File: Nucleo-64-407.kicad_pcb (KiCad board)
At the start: 2 copper layers, 70 x 81 mm, 70 parts, among them J1 SWD, J2 Micro_SD_Card_Det, J3 USB_B_Micro, J4 Serial 0, J5 EXP1, J6 EXP2, J7 EXP3, J8 EXP4, SW1 RESET, SW2 BOOT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

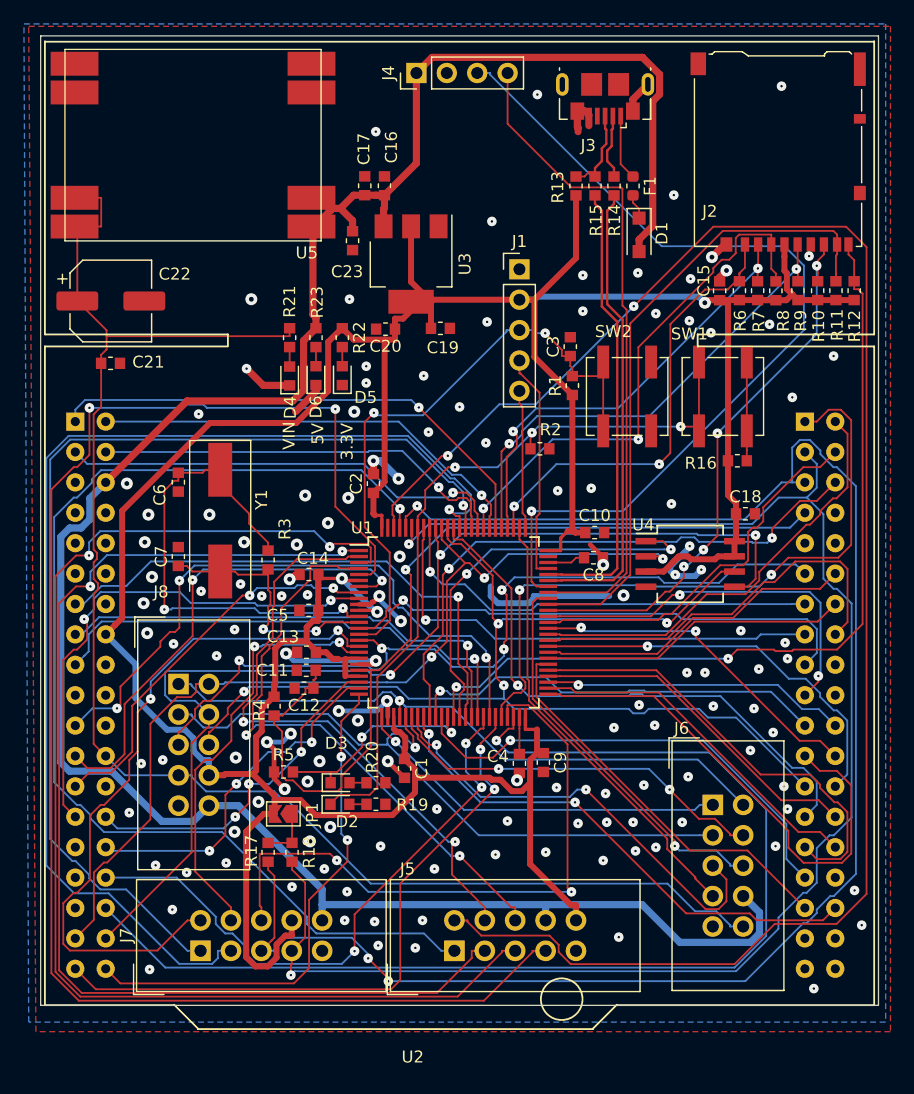
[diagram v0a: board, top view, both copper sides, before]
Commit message: Ordered rev1 of the Nucleo-64 board.
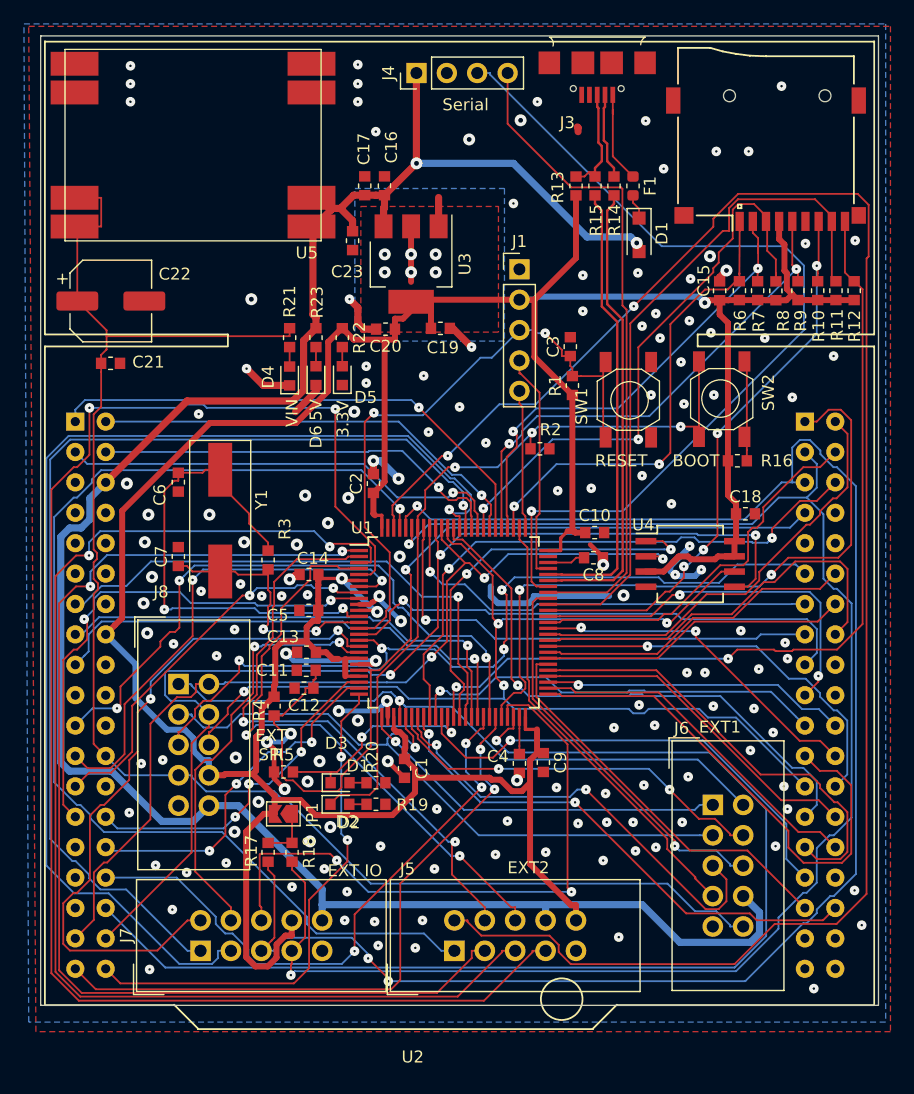
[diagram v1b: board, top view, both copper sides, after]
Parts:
- removed J2: Micro_SD_Card_Det, Connector_Card:microSD_HC_Hirose_DM3AT-SF-PEJM5
- added XS1: MicroSD, PrntrBoardV1:Conn_uSDcard, F.Cu at (113.6, 40.0)
- J3: footprint Connector_USB:USB_Micro-B_GCT_USB3076-30-A -> PrntrBoardV1:MC-101C
- SW1, SW2: footprint Button_Switch_SMD:SW_SPST_B3SL-1002P -> PrntrBoardV1:Button 4x4
- moved SW2 3.92 mm to (108.0, 68.5)
- moved SW1 3.50 mm to (104.0, 62.2)
- moved J3 1.20 mm to (99.5, 39.2)
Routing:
- net /5V: track 195.0 -> 180.0 mm, vias 0 -> 2
- net /IOE_1: track 144.7 -> 149.7 mm
- net /SDIO_CMD: track 44.7 -> 49.3 mm
- net /SDIO_D1: track 53.4 -> 57.3 mm
- net /SDIO_D3: track 37.7 -> 40.6 mm
- net Net-(F1-Pad1): track 5.47 -> 7.85 mm
- net /D+: track 7.21 -> 9.31 mm
- net /SDIO_CLK: track 40.7 -> 42.7 mm
- net /SD_DETECT: track 71.2 -> 73.1 mm
- net /SDIO_D0: track 46.6 -> 48.4 mm
- net /D-: track 5.48 -> 7.22 mm
- net /SDIO_D2: track 38.1 -> 39.9 mm
- net /3.3V: track 316.1 -> 317.8 mm, vias 3 -> 9
- net GND: track 71.2 -> 71.9 mm, vias 134 -> 153
- added copper zone on B.Cu, net /3.3V
- added copper zone on F.Cu, net /3.3V
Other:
- board text added: "BOOT"
- board text added: "D1"
- board text added: "D2"
- board text added: "EXT IO"
- board text added: "IOA 3,5,7,15"
- board text added: "IOA 4"
- board text added: "IOA 4,6,8"
- board text added: "IOA 5"
- board text added: "IOE 0,2,4,6"
- board text added: "IOE 1,3,5"
- board text added: "MISO"
- board text added: "MOSI"
- board text added: "RESET"
- board text added: "SCK"
- board text added: "SCL"
- board text added: "SDA"
- board text added: "Serial"
- board text added: "~EN_MOT"

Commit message: Make the NUCLEO-64-F407 board with rounded corners.
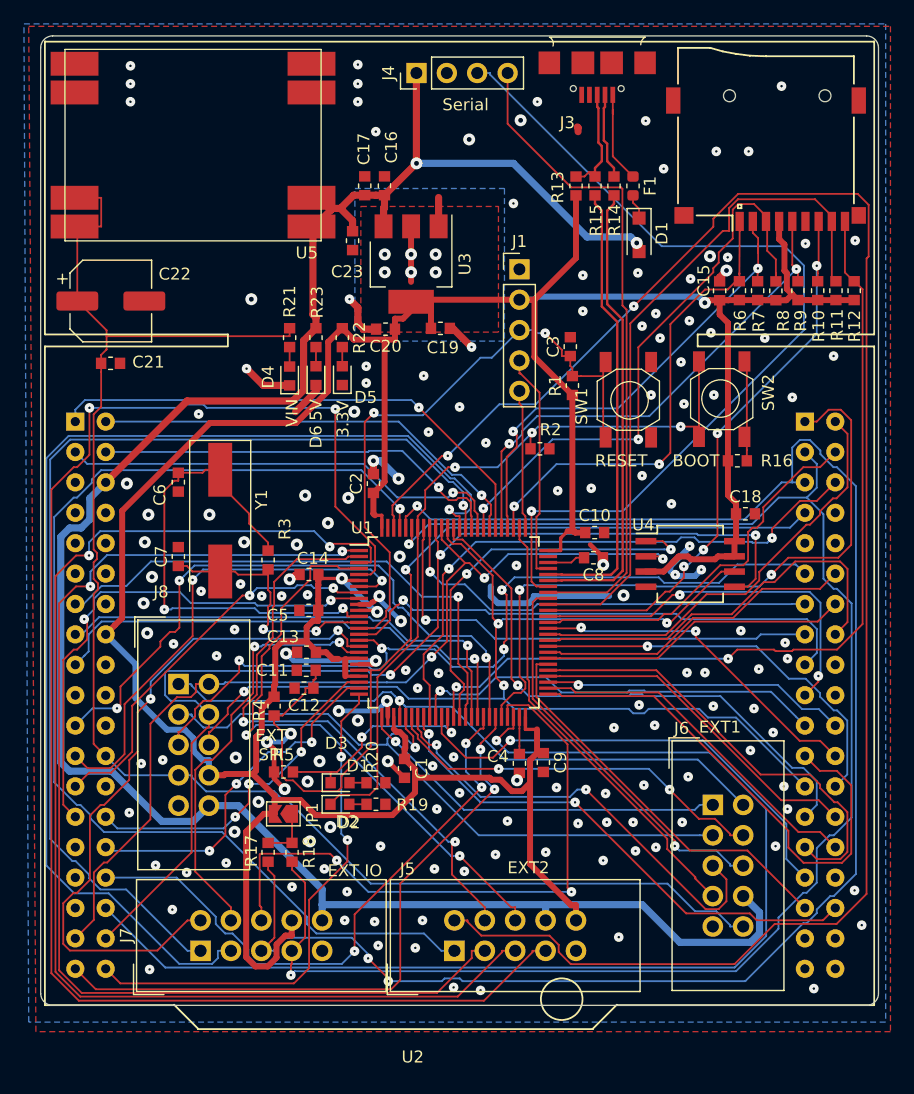
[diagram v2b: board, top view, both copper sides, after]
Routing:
- net GND: vias 153 -> 164
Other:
- outline, holes or cut-outs redrawn
- board text added: "(c) iQury.us Dec 2018"
- board text added: "Rev 2"
- board text removed: "(c) iQury.us Nov 2018"
- board text removed: "Rev1"
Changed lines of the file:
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@@
-(kicad_pcb (version 20171130) (host pcbnew 6.0.0-rc1-unknown-82f657e~66~ubuntu18.10.1)
+(kicad_pcb (version 20171130) (host pcbnew 6.0.0-rc1-unknown-0bceb69~66~ubuntu18.10.1)
   (general
     (thickness 1.6)
-    (drawings 62)
-    (tracks 1999)
+    (drawings 66)
+    (tracks 2014)
     (zones 0)
     (modules 70)
@@
     (via_min_size 0.8)
     (via_min_drill 0.2)
+    (user_via 0.8 0.2)
+    (user_via 1 0.4)
     (uvia_size 0.3)
     (uvia_drill 0.1)
@@
     )
   )
+  (gr_arc (start 54 115) (end 53 115) (angle -90) (layer Edge.Cuts) (width 0.05))
+  (gr_arc (start 122 115) (end 122 116) (angle -90) (layer Edge.Cuts) (width 0.05))
+  (gr_arc (start 122 36) (end 123 36) (angle -90) (layer Edge.Cuts) (width 0.05))
+  (gr_arc (start 54 36) (end 54 35) (angle -90) (layer Edge.Cuts) (width 0.05))
   (gr_text "EXT\nSPI" (at 72.25 94.25) (layer F.SilkS)
     (effects (font (size 1 1) (thickness 0.15)))
@@
     (effects (font (size 1 1) (thickness 0.15)) (justify mirror))
   )
-  (gr_text Rev1 (at 114.2 42) (layer B.SilkS)
+  (gr_text "Rev 2" (at 114.2 42) (layer B.SilkS)
     (effects (font (size 1.5 1.5) (thickness 0.3)) (justify mirror))
   )
-  (gr_text "(c) iQury.us\nNov 2018" (at 66.6 51.3) (layer B.SilkS)
+  (gr_text "(c) iQury.us\nDec 2018" (at 66.6 51.3) (layer B.SilkS)
     (effects (font (size 1.5 1.5) (thickness 0.3)) (justify mirror))
   )
@@
     (effects (font (size 1.5 1.5) (thickness 0.3)) (justify mirror))
   )
-  (gr_line (start 53 116) (end 53 35) (layer Edge.Cuts) (width 0.05))
-  (gr_line (start 123 116) (end 53 116) (layer Edge.Cuts) (width 0.05))
-  (gr_line (start 123 35) (end 123 116) (layer Edge.Cuts) (width 0.05))
-  (gr_line (start 53 35) (end 123 35) (layer Edge.Cuts) (width 0.05))
+  (gr_line (start 53 115) (end 53 36) (layer Edge.Cuts) (width 0.05))
+  (gr_line (start 122 116) (end 54 116) (layer Edge.Cuts) (width 0.05))
+  (gr_line (start 123 36) (end 123 115) (layer Edge.Cuts) (width 0.05))
+  (gr_line (start 54 35) (end 122 35) (layer Edge.Cuts) (width 0.05))
   (segment (start 94.2 81.8) (end 94.2 82) (width 0.5) (layer B.Cu) (net 1))
   (segment (start 94.2 82) (end 93.8 82.4) (width 0.5) (layer B.Cu) (net 1))
@@
   (via (at 104.75 60.25) (size 0.8) (drill 0.2) (layers F.Cu B.Cu) (net 1))
   (via (at 103.25 59.25) (size 0.8) (drill 0.2) (layers F.Cu B.Cu) (net 1))
+  (via (at 89.75 114.75) (size 0.8) (drill 0.2) (layers F.Cu B.Cu) (net 1))
+  (via (at 87.5 114.5) (size 0.8) (drill 0.2) (layers F.Cu B.Cu) (net 1))
+  (via (at 88 98.25) (size 0.8) (drill 0.2) (layers F.Cu B.Cu) (net 1))
+  (via (at 85.75 96) (size 0.8) (drill 0.2) (layers F.Cu B.Cu) (net 1))
+  (via (at 87.5 95.25) (size 0.8) (drill 0.2) (layers F.Cu B.Cu) (net 1))
+  (via (at 84.5 89.5) (size 0.8) (drill 0.2) (layers F.Cu B.Cu) (net 1))
+  (via (at 83.5 88) (size 0.8) (drill 0.2) (layers F.Cu B.Cu) (net 1))
+  (via (at 86.25 88.25) (size 0.8) (drill 0.2) (layers F.Cu B.Cu) (net 1))
+  (via (at 92.75 79.25) (size 0.8) (drill 0.2) (layers F.Cu B.Cu) (net 1))
+  (via (at 88.4 104.8) (size 0.8) (drill 0.2) (layers F.Cu B.Cu) (net 1))
+  (via (at 110.4 53.5) (size 0.8) (drill 0.2) (layers F.Cu B.Cu) (net 1))
   (segment (start 95.4 78) (end 96.4426 78) (width 0.2798) (layer F.Cu) (net 2))
   (segment (start 97.0174 76.3826) (end 96.4426 76.9574) (width 0.2798) (layer F.Cu) (net 2))
@@
   (via (at 97.3457 106.5181) (size 0.8) (layers F.Cu B.Cu) (net 40))
   (segment (start 115.7899 72.305) (end 116.8515 72.305) (width 0.1524) (layer B.Cu) (net 41))
-  (segment (start 82.0448 113.9811) (end 111.8717 113.9811) (width 0.1524) (layer B.Cu) (net 41))
-  (segment (start 111.8717 113.9811) (end 116.7178 109.135) (width 0.1524) (layer B.Cu) (net 41))
-  (segment (start 116.7178 109.135) (end 117.0008 109.135) (width 0.1524) (layer B.Cu) (net 41))
-  (segment (start 117.0008 109.135) (end 117.8426 108.2932) (width 0.1524) (layer B.Cu) (net 41))
-  (segment (start 117.8426 108.2932) (end 117.8426 107.9947) (width 0.1524) (layer B.Cu) (net 41))
-  (segment (start 117.8426 107.9947) (end 118.9634 106.8739) (width 0.1524) (layer B.Cu) (net 41))
-  (segment (start 118.9634 106.8739) (end 119.2567 106.8739) (width 0.1524) (layer B.Cu) (net 41))
-  (segment (start 119.2567 106.8739) (end 121.114 105.0166) (width 0.1524) (layer B.Cu) (net 41))
-  (segment (start 121.114 105.0166) (end 121.114 72.6223) (width 0.1524) (layer B.Cu) (net 41))
-  (segment (start 121.114 72.6223) (end 119.5267 71.035) (width 0.1524) (layer B.Cu) (net 41))
-  (segment (start 119.5267 71.035) (end 119.2413 71.035) (width 0.1524) (layer B.Cu) (net 41))
-  (segment (start 119.2413 71.035) (end 118.1477 69.9414) (width 0.1524) (layer B.Cu) (net 41))
-  (segment (start 118.1477 69.9414) (end 118.1477 69.6488) (width 0.1524) (layer B.Cu) (net 41))
-  (segment (start 118.1477 69.6488) (end 117.2604 68.7615) (width 0.1524) (layer B.Cu) (net 41))
-  (segment (start 117.2604 68.7615) (end 116.4271 68.7615) (width 0.1524) (layer B.Cu) (net 41))
-  (segment (start 116.4271 68.7615) (end 115.7899 69.3987) (width 0.1524) (layer B.Cu) (net 41))
-  (segment (start 115.7899 69.3987) (end 115.7899 72.305) (width 0.1524) (layer B.Cu) (net 41))
   (segment (start 115.7899 72.305) (end 114.9035 72.305) (width 0.1524) (layer B.Cu) (net 41))
   (segment (start 114.9035 72.305) (end 111.8107 75.3978) (width 0.1524) (layer B.Cu) (net 41))
@@
   (segment (start 72.529701 110.349799) (end 72.301099 110.578401) (width 0.1524) (layer F.Cu) (net 41))
   (segment (start 72 104.6659) (end 72.529701 105.195601) (width 0.1524) (layer F.Cu) (net 41))
+  (segment (start 115.7899 69.3987) (end 115.7899 72.305) (width 0.1524) (layer B.Cu) (net 41))
+  (segment (start 116.4271 68.7615) (end 115.7899 69.3987) (width 0.1524) (layer B.Cu) (net 41))
+  (segment (start 117.2604 68.7615) (end 116.4271 68.7615) (width 0.1524) (layer B.Cu) (net 41))
+  (segment (start 118.1477 69.6488) (end 117.2604 68.7615) (width 0.1524) (layer B.Cu) (net 41))
+  (segment (start 111.8717 113.9811) (end 116.7178 109.135) (width 0.1524) (layer B.Cu) (net 41))
+  (segment (start 88.25 113.9811) (end 111.8717 113.9811) (width 0.1524) (layer B.Cu) (net 41))
+  (segment (start 86.75 113.75) (end 88.0189 113.75) (width 0.1524) (layer B.Cu) (net 41))
+  (segment (start 119.2567 106.8739) (end 121.114 105.0166) (width 0.1524) (layer B.Cu) (net 41))
+  (segment (start 86.5189 113.9811) (end 86.75 113.75) (width 0.1524) (layer B.Cu) (net 41))
+  (segment (start 82.0448 113.9811) (end 86.5189 113.9811) (width 0.1524) (layer B.Cu) (net 41))
+  (segment (start 116.7178 109.135) (end 117.0008 109.135) (width 0.1524) (layer B.Cu) (net 41))
+  (segment (start 118.1477 69.9414) (end 118.1477 69.6488) (width 0.1524) (layer B.Cu) (net 41))
+  (segment (start 117.8426 108.2932) (end 117.8426 107.9947) (width 0.1524) (layer B.Cu) (net 41))
+  (segment (start 119.5267 71.035) (end 119.2413 71.035) (width 0.1524) (layer B.Cu) (net 41))
+  (segment (start 117.8426 107.9947) (end 118.9634 106.8739) (width 0.1524) (layer B.Cu) (net 41))
+  (segment (start 88.0189 113.75) (end 88.25 113.9811) (width 0.1524) (layer B.Cu) (net 41))
+  (segment (start 121.114 105.0166) (end 121.114 72.6223) (width 0.1524) (layer B.Cu) (net 41))
+  (segment (start 118.9634 106.8739) (end 119.2567 106.8739) (width 0.1524) (layer B.Cu) (net 41))
+  (segment (start 121.114 72.6223) (end 119.5267 71.035) (width 0.1524) (layer B.Cu) (net 41))
+  (segment (start 117.0008 109.135) (end 117.8426 108.2932) (width 0.1524) (layer B.Cu) (net 41))
+  (segment (start 119.2413 71.035) (end 118.1477 69.9414) (width 0.1524) (layer B.Cu) (net 41))
   (segment (start 68.8975 107.8095) (end 65.9138 104.8258) (width 0.1524) (layer F.Cu) (net 42))
   (segment (start 65.9138 104.8258) (end 65.9138 96.3229) (width 0.1524) (layer F.Cu) (net 42))

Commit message: Improve the NUCLEO-64 layout a bit.
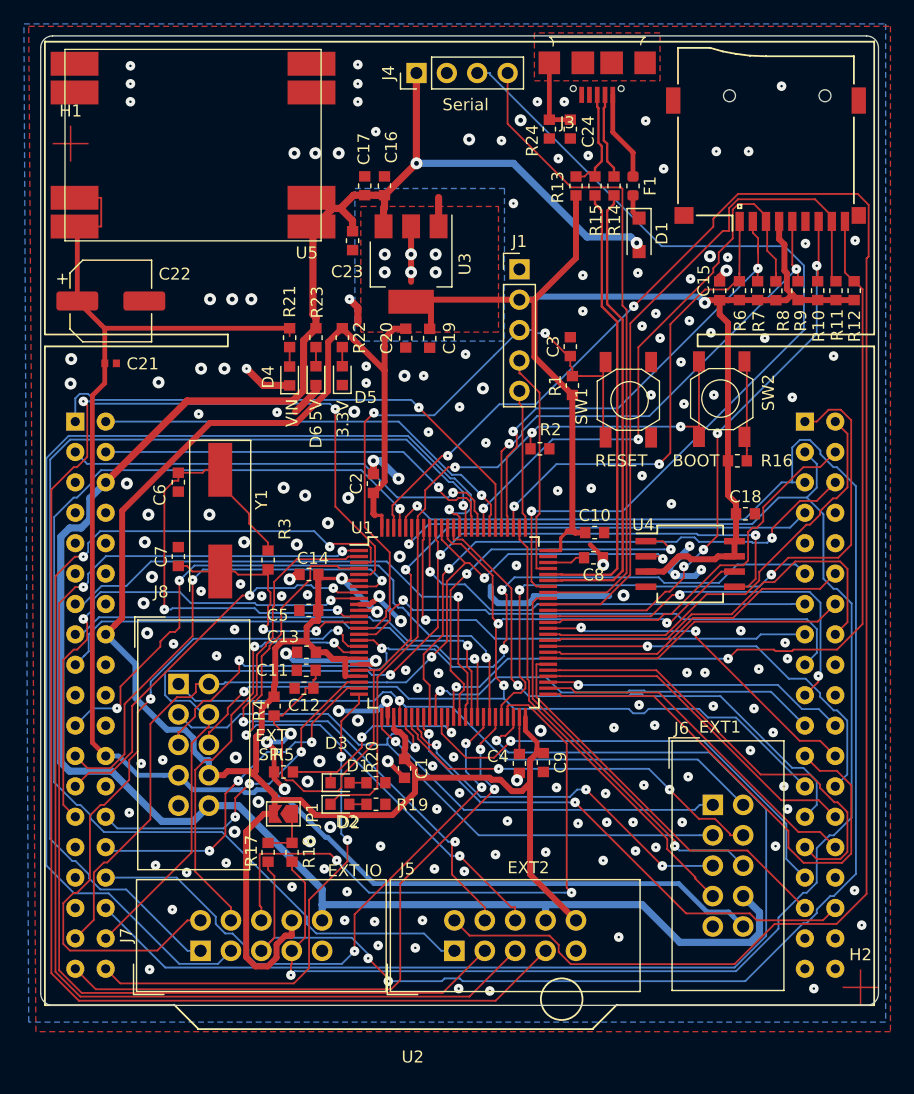
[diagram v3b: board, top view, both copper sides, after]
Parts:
- added C24: 0.1uF, PrntrBoardV1:C_0603_1608Metric, F.Cu at (97.2, 42.8)
- added H1: FID1, PrntrBoardV1:Fiducial_1mm_Dia_2.54mm_Outer_CopperTop, F.Cu at (55.5, 44.0)
- added H2: FID2, PrntrBoardV1:Fiducial_1mm_Dia_2.54mm_Outer_CopperTop, F.Cu at (121.5, 114.5)
- added R24: 100k, PrntrBoardV1:R_0603_1608Metric, F.Cu at (95.5, 42.8)
- C21: footprint PrntrBoardV1:C_0603_1608Metric -> PrntrBoardV1:C_0402_1005Metric
- moved C20 1.85 mm to (83.5, 60.2), turned to 270 degrees
- moved C19 1.22 mm to (85.5, 60.3), turned to 270 degrees
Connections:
- J3 pad 6: GND -> Net-(C24-Pad2)
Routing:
- net Net-(C24-Pad2): track 0.00 -> 6.50 mm
- net /IOA_7: track 37.9 -> 31.5 mm, vias 2 -> 3
- net /VIN: track 129.1 -> 135.1 mm
- net GND: track 71.9 -> 67.3 mm, vias 164 -> 183
- net /3.3V: track 317.8 -> 315.2 mm
- net /IOE_6: track 129.9 -> 130.9 mm
- net /X_START: track 43.0 -> 44.0 mm
- net /IOE_2: track 96.4 -> 95.8 mm
- added copper zone on F.Cu, net Net-(C24-Pad2)
